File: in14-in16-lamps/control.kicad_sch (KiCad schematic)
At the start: 22 parts, among them J2 Conn_01x02_Pin, J3 Conn_01x06_Pin, Q10 2N7002, SW1 SW_Push, U3 ESP32-WROOM-32D, U4 DS3231M, U5 74141

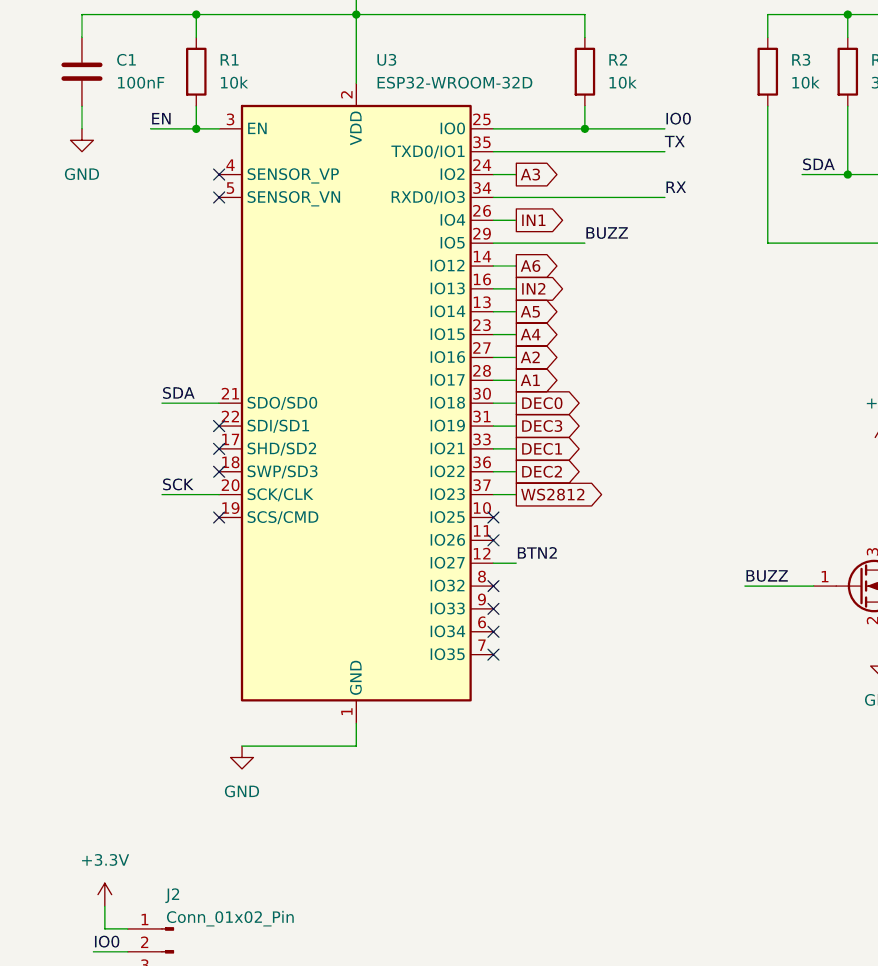
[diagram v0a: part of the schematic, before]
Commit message: fix i2c connection
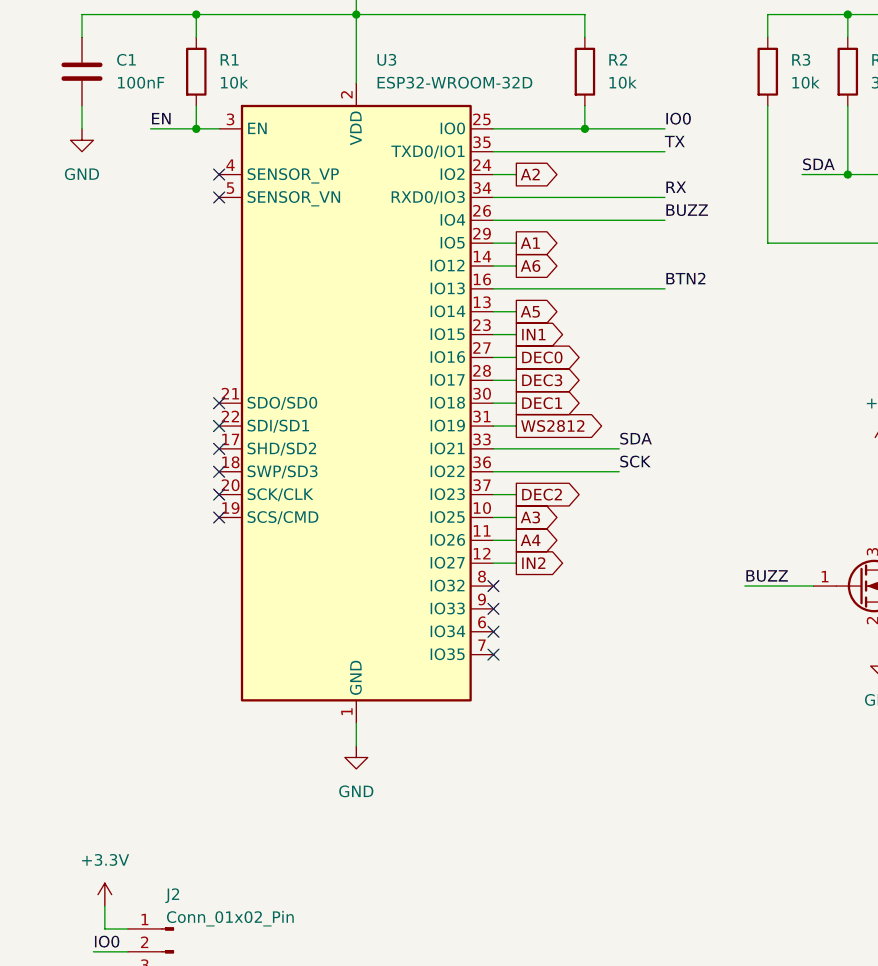
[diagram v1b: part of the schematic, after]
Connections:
- net A1: now also U3.29 (IO5); no longer U3.28 (IO17)
- net A2: now also U3.24 (IO2); no longer U3.27 (IO16)
- net A3: now also U3.10 (IO25); no longer U3.24 (IO2)
- net A4: now also U3.11 (IO26); no longer U3.23 (IO15)
- net BTN2: now also U3.16 (IO13); no longer U3.12 (IO27)
- net BUZZ: now also U3.26 (IO4); no longer U3.29 (IO5)
- net DEC0: now also U3.27 (IO16); no longer U3.30 (IO18)
- net DEC1: now also U3.30 (IO18); no longer U3.33 (IO21)
- net DEC2: now also U3.37 (IO23); no longer U3.36 (IO22)
- net DEC3: now also U3.28 (IO17); no longer U3.31 (IO19)
- net IN1: now also U3.23 (IO15); no longer U3.26 (IO4)
- net IN2: now also U3.12 (IO27); no longer U3.16 (IO13)
- net SCK: now also U3.36 (IO22); no longer U3.20 (SCK/CLK)
- net SDA: now also U3.33 (IO21); no longer U3.21 (SDO/SD0)
- net WS2812: now also U3.31 (IO19); no longer U3.37 (IO23)
